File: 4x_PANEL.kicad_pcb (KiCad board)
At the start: 2 copper layers, 88.4 x 99.2 mm, 8 parts, among them J1 SCART-F, J2 SCART-F

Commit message: Renamed all gerbers and files to match
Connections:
- J2 pad 10: S_IN -> S_OUT (x4)
- J2 pad 9: S_OUT -> S_IN (x4)
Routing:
- net S_IN: track 151.2 -> 167.1 mm, vias 0 -> 4
- net S_OUT: track 137.2 -> 138.0 mm, vias 2 -> 6
- net GND: vias 156 -> 152

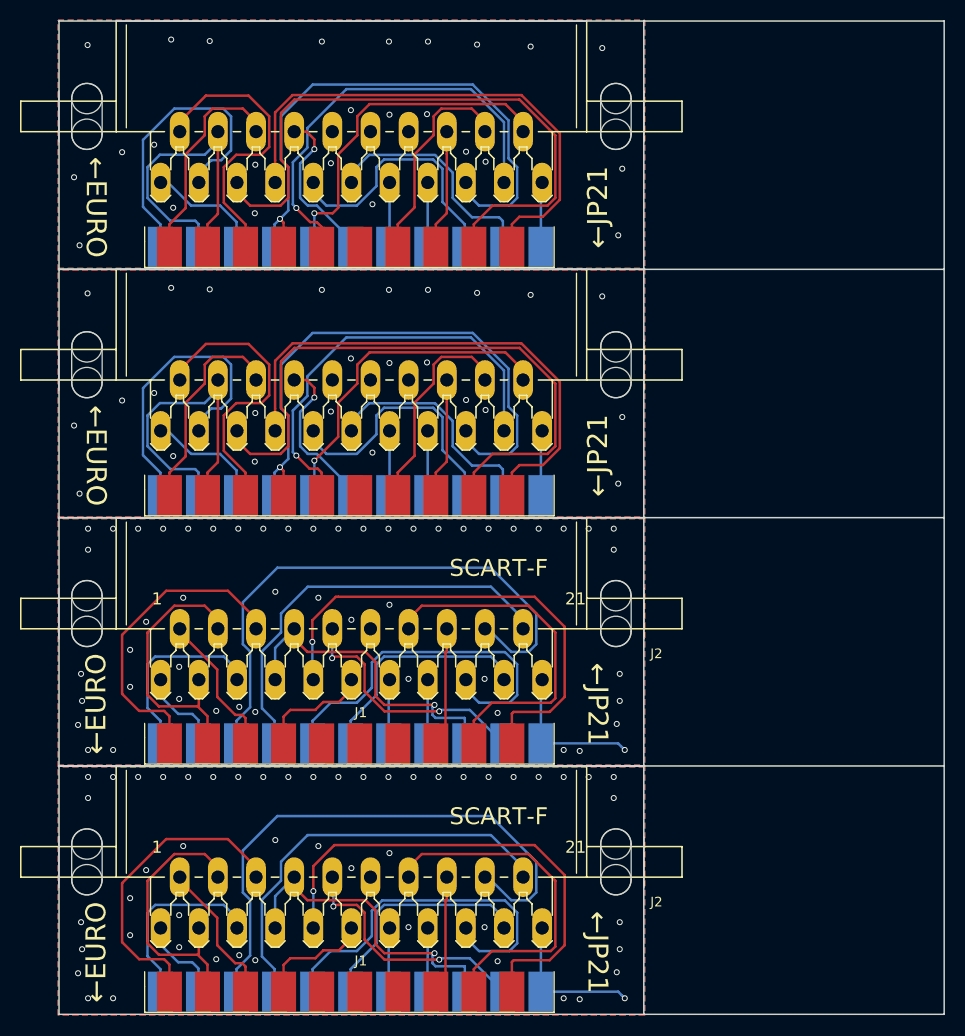
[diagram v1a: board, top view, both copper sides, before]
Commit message: fixed incorrect audio pins for JP21
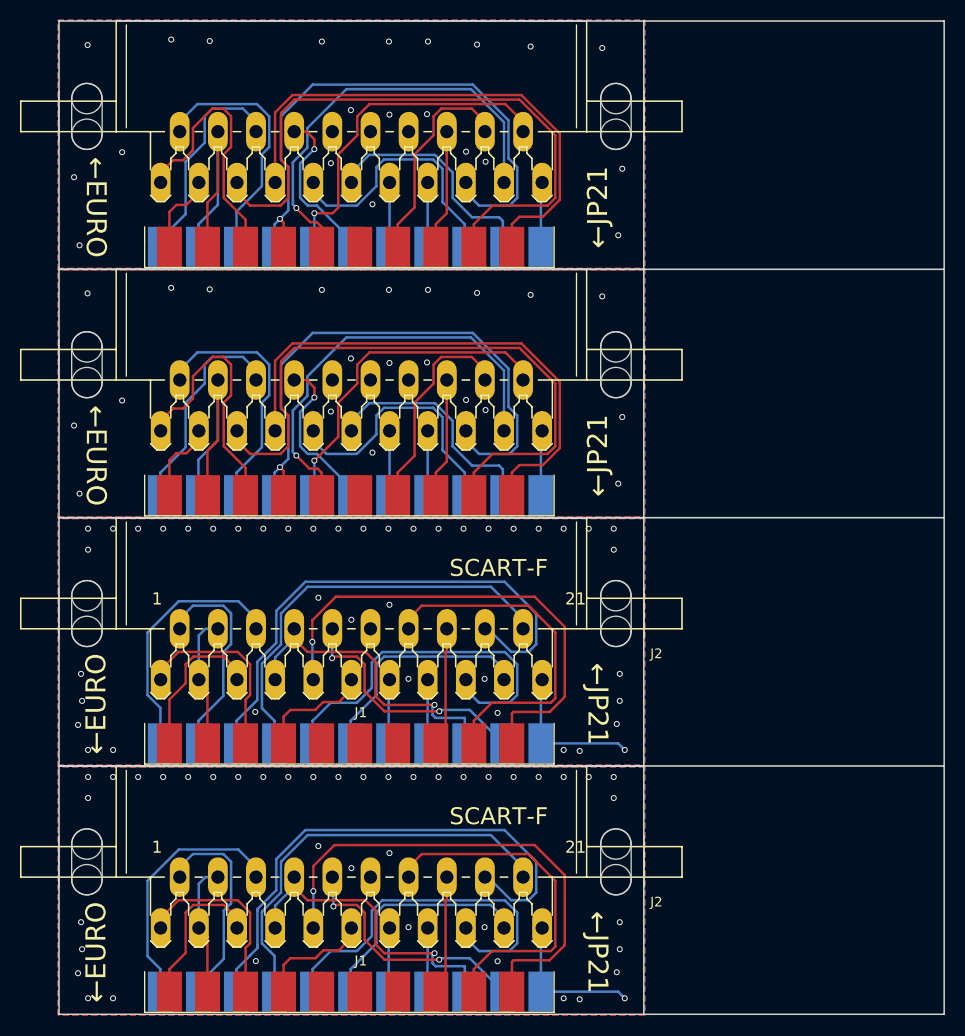
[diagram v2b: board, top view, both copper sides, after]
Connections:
- J2 pad 1: L_OUT -> L_IN (x4)
- J2 pad 2: L_IN -> L_OUT (x4)
- J2 pad 5: RT_OUT -> RT_IN (x4)
- J2 pad 6: RT_IN -> RT_OUT (x4)
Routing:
- net A_GND: track 123.5 -> 77.1 mm
- net RT_OUT: track 61.8 -> 104.0 mm
- net RT_IN: track 121.5 -> 82.2 mm
- net L_OUT: track 78.2 -> 59.0 mm
- net L_IN: track 72.1 -> 82.2 mm
- net B_GND: track 241.5 -> 233.0 mm
- net GND: vias 152 -> 126
